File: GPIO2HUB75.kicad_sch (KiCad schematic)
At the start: 3 parts, among them J1 Conn_02x10_Odd_Even, J2 Conn_02x20_Odd_Even_MountingP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, J3 Conn_02x08_Top_Bottom

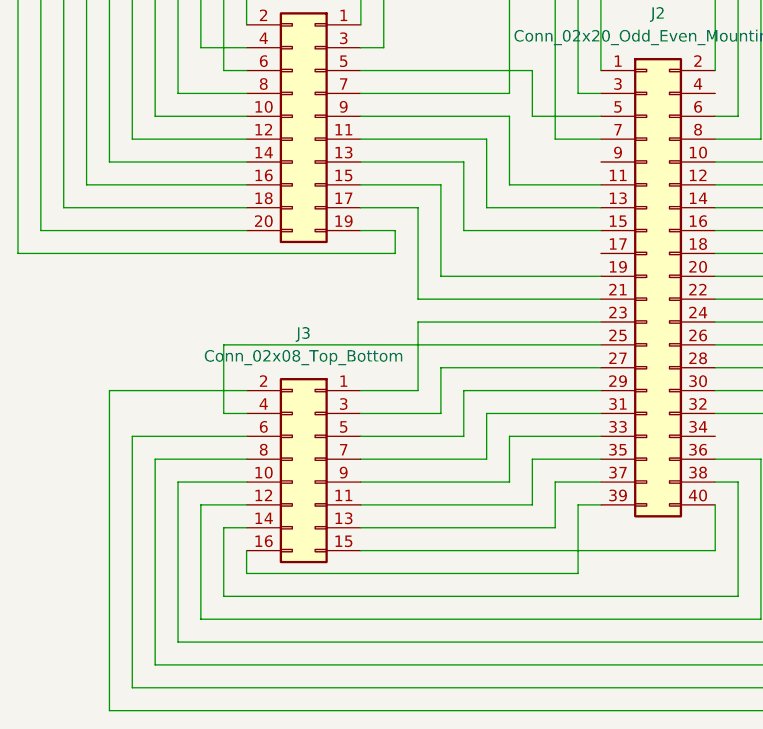
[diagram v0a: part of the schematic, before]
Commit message: added solder bridge to support 64x64+ panels
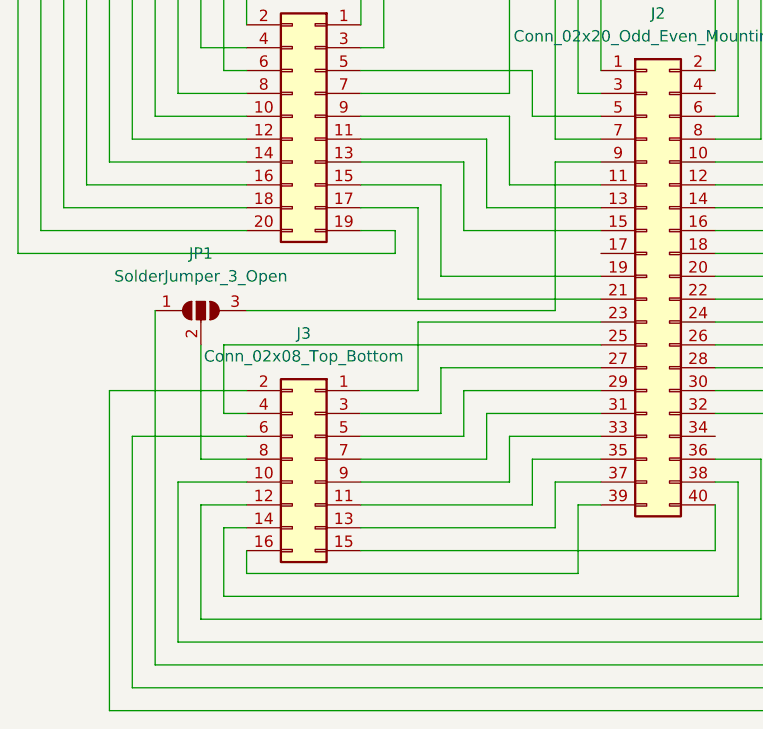
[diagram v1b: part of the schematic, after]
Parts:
- added JP1: SolderJumper_3_Open, Jumper:SolderJumper-3_P1.3mm_Open_Pad1.0x1.5mm_NumberLabels, symbol Jumper:SolderJumper_3_Open
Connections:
- net at J2.28 (Pin_28): now also JP1.1 (A); no longer J3.8 (Pin_8)
- net at J2.9 (Pin_9): now also JP1.3 (B)
- new net: J3.8 (Pin_8), JP1.2 (C)
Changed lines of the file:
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@@
+    (stroke (width 0) (type default))
+  )
+  (wire (pts (xy 193.04 72.39) (xy 187.96 72.39))
     (stroke (width 0) (type default))
   )
@@
     (stroke (width 0) (type default))
   )
-  (wire (pts (xy 143.51 105.41) (xy 143.51 128.27))
-    (stroke (width 0) (type default))
-  )
   (wire (pts (xy 205.74 62.23) (xy 205.74 48.26))
     (stroke (width 0) (type default))
@@
     (stroke (width 0) (type default))
   )
-  (wire (pts (xy 143.51 105.41) (xy 153.67 105.41))
-    (stroke (width 0) (type default))
-  )
   (wire (pts (xy 185.42 62.23) (xy 166.37 62.23))
     (stroke (width 0) (type default))
@@
     (stroke (width 0) (type default))
   )
+  (wire (pts (xy 148.59 105.41) (xy 153.67 105.41))
+    (stroke (width 0) (type default))
+  )
   (wire (pts (xy 205.74 90.17) (xy 220.98 90.17))
     (stroke (width 0) (type default))
@@
     (stroke (width 0) (type default))
   )
+  (wire (pts (xy 143.51 88.9) (xy 143.51 128.27))
+    (stroke (width 0) (type default))
+  )
   (wire (pts (xy 193.04 62.23) (xy 193.04 45.72))
     (stroke (width 0) (type default))
@@
     (stroke (width 0) (type default))
   )
+  (wire (pts (xy 148.59 92.71) (xy 148.59 105.41))
+    (stroke (width 0) (type default))
+  )
   (wire (pts (xy 146.05 125.73) (xy 213.36 125.73))
     (stroke (width 0) (type default))
@@
     (stroke (width 0) (type default))
   )
+  (wire (pts (xy 153.67 88.9) (xy 187.96 88.9))
+    (stroke (width 0) (type default))
+  )
   (wire (pts (xy 170.18 80.01) (xy 166.37 80.01))
     (stroke (width 0) (type default))
   )
+  (wire (pts (xy 187.96 72.39) (xy 187.96 88.9))
+    (stroke (width 0) (type default))
+  )
   (wire (pts (xy 135.89 27.94) (xy 135.89 74.93))
     (stroke (width 0) (type default))
@@
     (stroke (width 0) (type default))
   )
+  (symbol (lib_id "Jumper:SolderJumper_3_Open") (at 148.59 88.9 0) (unit 1)
+    (in_bom yes) (on_board yes) (dnp no) (fields_autoplaced)
+    (property "Reference" "JP1" (at 148.59 82.55 0)
+      (effects (font (size 1.27 1.27)))
+    )
+    (property "Value" "SolderJumper_3_Open" (at 148.59 85.09 0)
+      (effects (font (size 1.27 1.27)))
+    )
+    (property "Footprint" "Jumper:SolderJumper-3_P1.3mm_Open_Pad1.0x1.5mm_NumberLabels" (at 148.59 88.9 0)
+      (effects (font (size 1.27 1.27)) hide)
+    )
+    (property "Datasheet" "~" (at 148.59 88.9 0)
+      (effects (font (size 1.27 1.27)) hide)
+    )
+    (pin "2")
+    (pin "1")
+    (pin "3")
+    (instances
+      (project "GPIO2HUB75"
+        (path "/1420b1a7-2230-482f-814a-7ef4eb1c7dc0"
+          (reference "JP1") (unit 1)
+        )
+      )
+    )
+  )
   (symbol (lib_id "Connector_Generic:Conn_02x08_Odd_Even") (at 161.29 105.41 0) (mirror y) (unit 1)

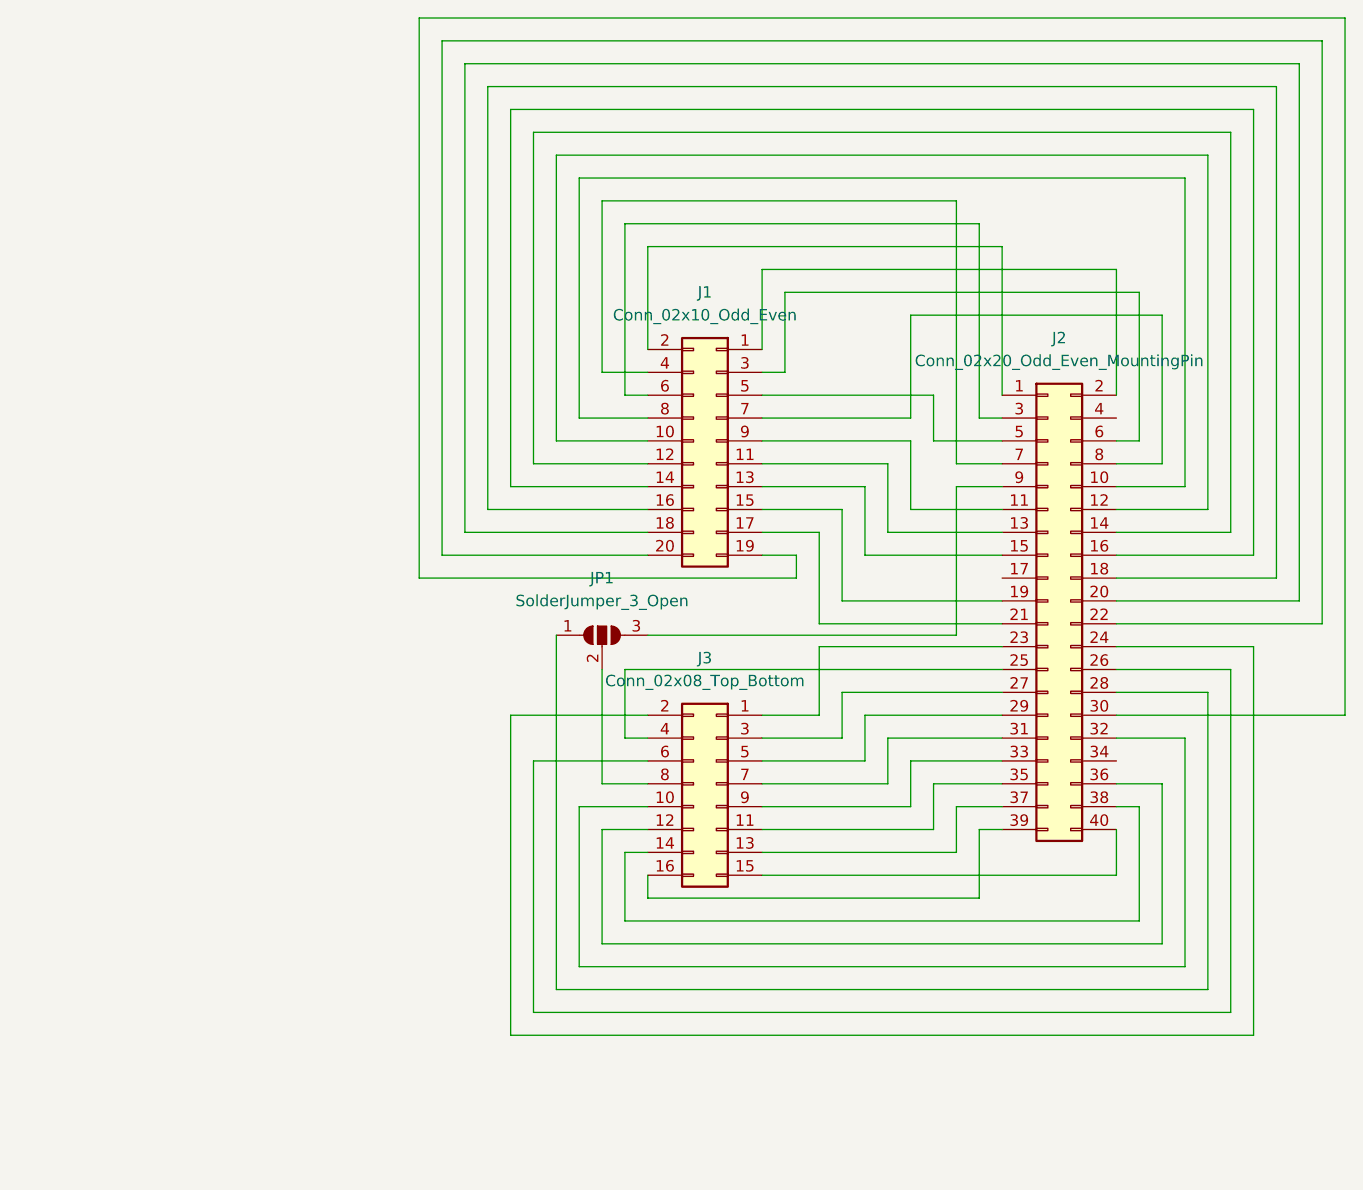
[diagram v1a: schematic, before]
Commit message: added a 3pin fan header
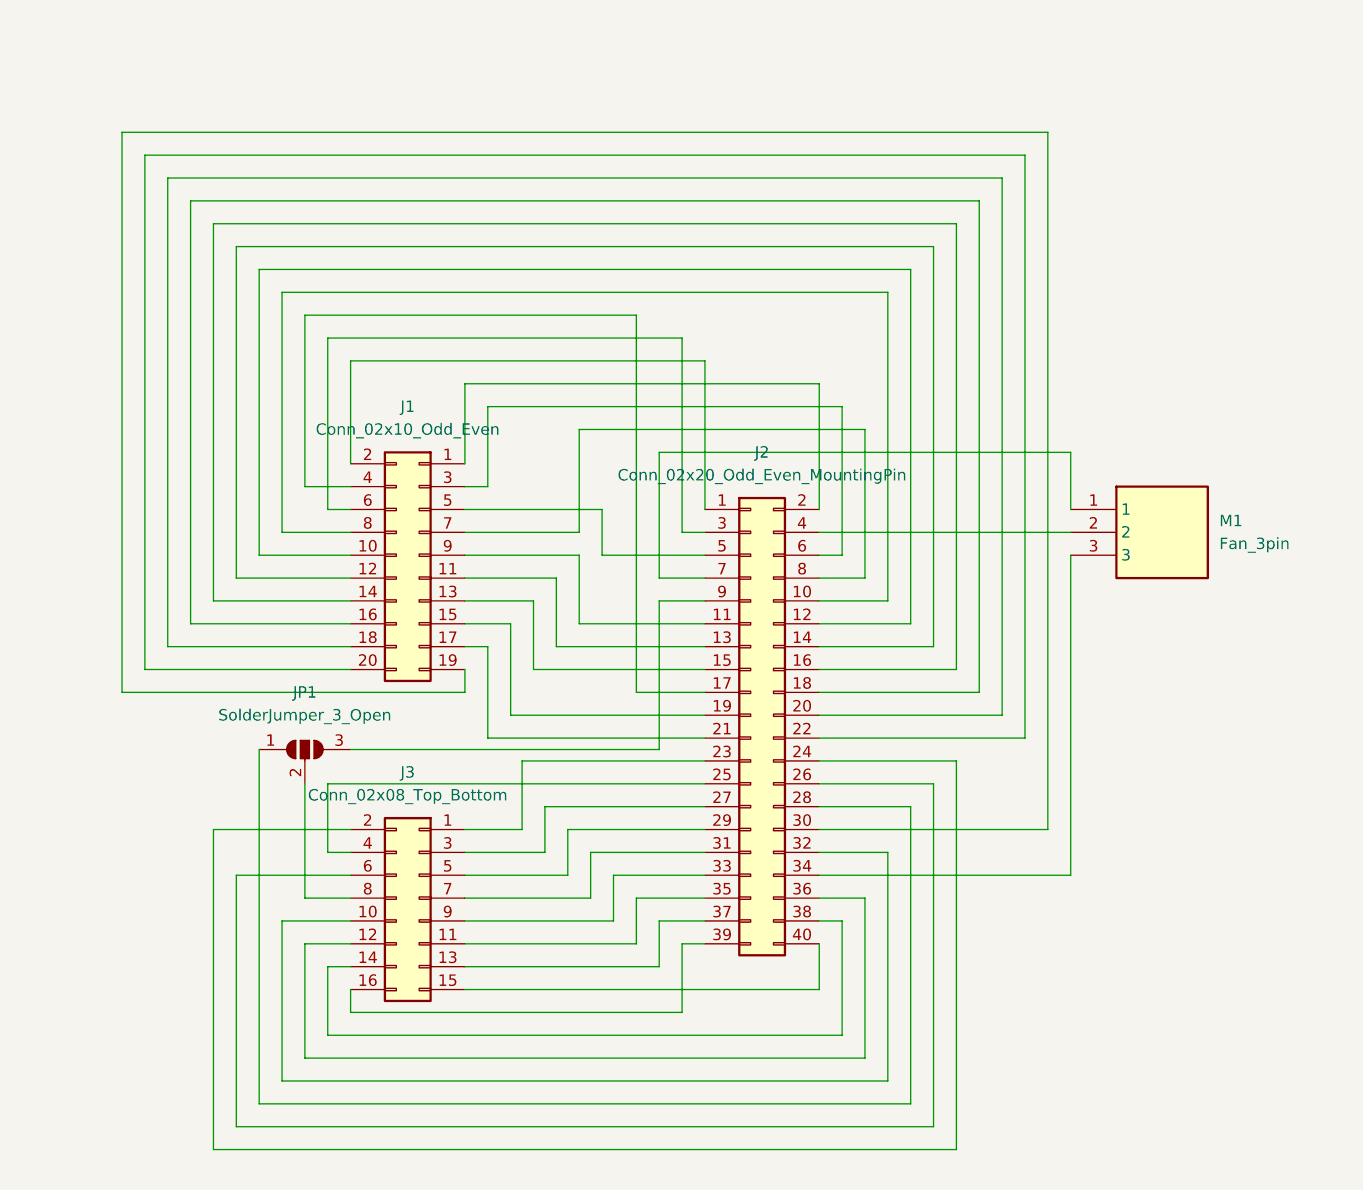
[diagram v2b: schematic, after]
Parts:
- added M1: Fan_3pin, 3 Pin Fan Header Angled:HDRRA3W64P0X254_1X3_747X318X635P, symbol 171857-3003:171857-3003
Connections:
- net at J2.17 (Pin_17): now also J1.4 (Pin_4)
- net at J2.34 (Pin_34): now also M1.3
- net at J2.4 (Pin_4): now also M1.2
- net at J2.7 (Pin_7): now also M1.1; no longer J1.4 (Pin_4)
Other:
- moved on the sheet: J1, J2, J3, JP1

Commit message: added a buzzer and split input pins from general GPIO
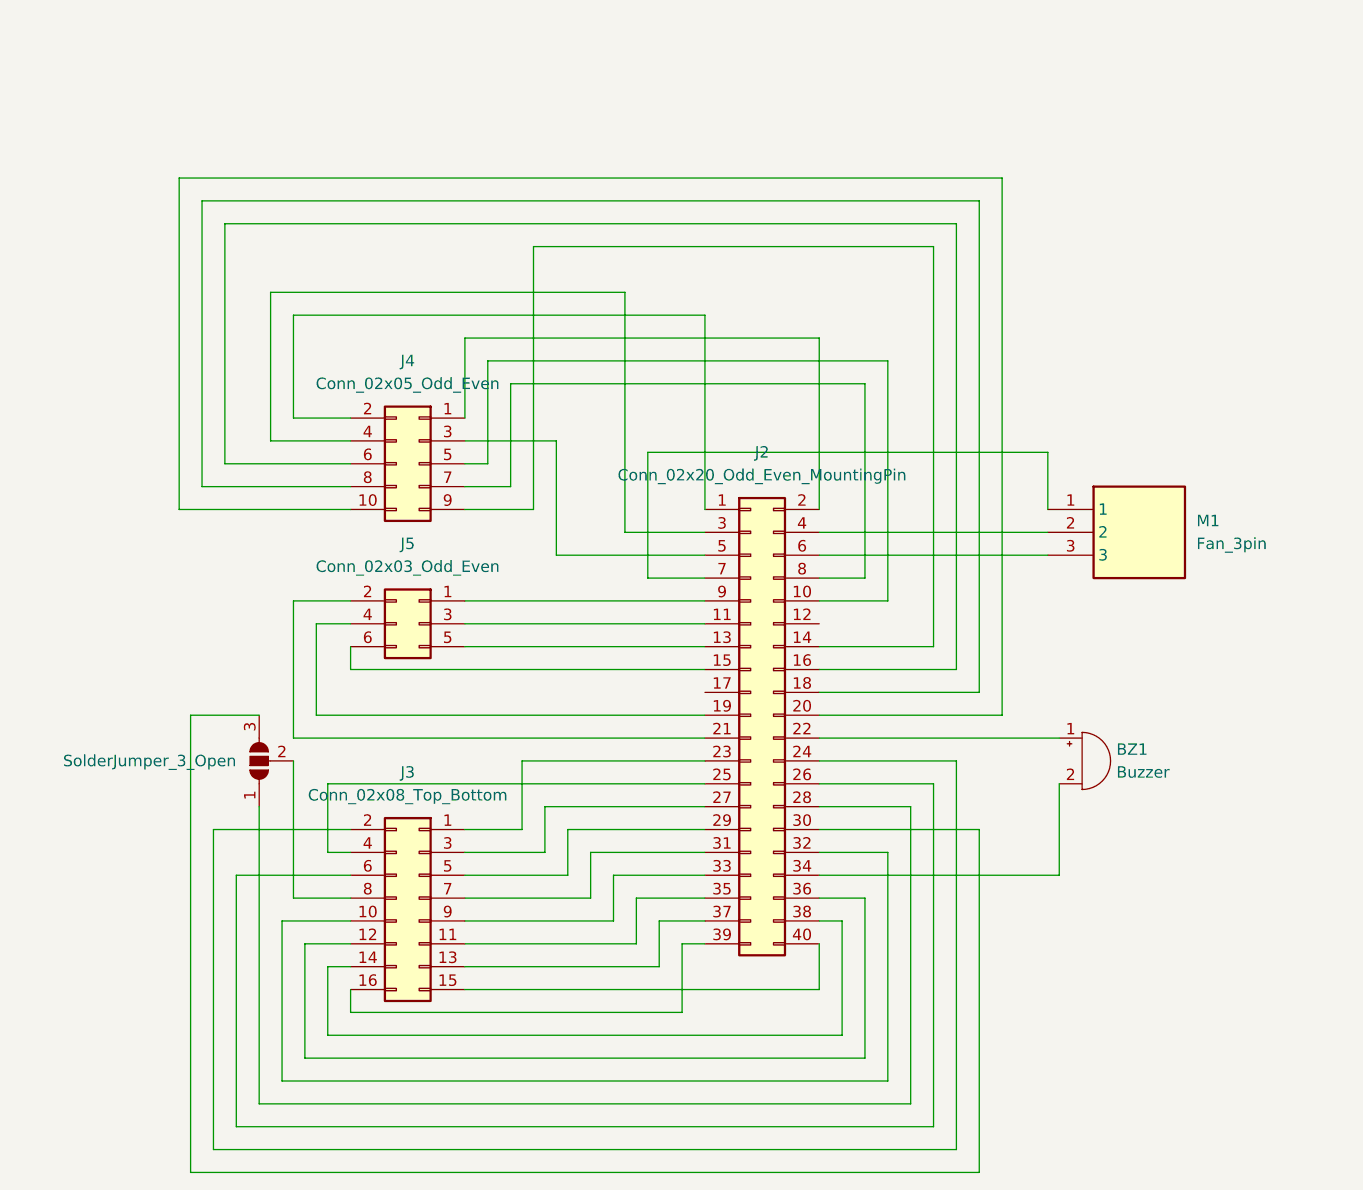
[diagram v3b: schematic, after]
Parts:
- removed J1: Conn_02x10_Odd_Even, Connector_PinHeader_2.54mm:PinHeader_2x10_P2.54mm_Horizontal, symbol Connector_Generic:Conn_02x10_Odd_Even
- added BZ1: Buzzer, Buzzer_Beeper:MagneticBuzzer_Kingstate_KCG0601, symbol Device:Buzzer
- added J4: Conn_02x05_Odd_Even, Connector_PinHeader_2.54mm:PinHeader_2x05_P2.54mm_Horizontal, symbol Connector_Generic:Conn_02x05_Odd_Even
- added J5: Conn_02x03_Odd_Even, Connector_IDC:IDC-Header_2x03_P2.54mm_Horizontal, symbol Connector_Generic:Conn_02x03_Odd_Even
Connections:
- net at J2.34 (Pin_34): now also BZ1.2 (+); no longer M1.3
- net at J2.9 (Pin_9): now also J5.1 (Pin_1); no longer JP1.3 (B)
- net at J2.1 (Pin_1): now also J4.2 (Pin_2)
- net at J2.10 (Pin_10): now also J4.5 (Pin_5)
- net at J2.11 (Pin_11): now also J5.3 (Pin_3)
- net at J2.13 (Pin_13): now also J5.5 (Pin_5)
- net at J2.14 (Pin_14): now also J4.9 (Pin_9)
- net at J2.15 (Pin_15): now also J5.6 (Pin_6)
- net at J2.16 (Pin_16): now also J4.6 (Pin_6)
- net at J2.18 (Pin_18): now also J4.8 (Pin_8)
- net at J2.19 (Pin_19): now also J5.4 (Pin_4)
- net at J2.2 (Pin_2): now also J4.1 (Pin_1)
- net at J2.20 (Pin_20): now also J4.10 (Pin_10)
- net at J2.21 (Pin_21): now also J5.2 (Pin_2)
- net at J2.22 (Pin_22): now also BZ1.1 (-)
- net at J2.3 (Pin_3): now also J4.4 (Pin_4)
- net at J2.30 (Pin_30): now also JP1.3 (B)
- net at J2.5 (Pin_5): now also J4.3 (Pin_3)
- net at J2.6 (Pin_6): now also M1.3
- net at J2.8 (Pin_8): now also J4.7 (Pin_7)
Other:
- moved on the sheet: M1

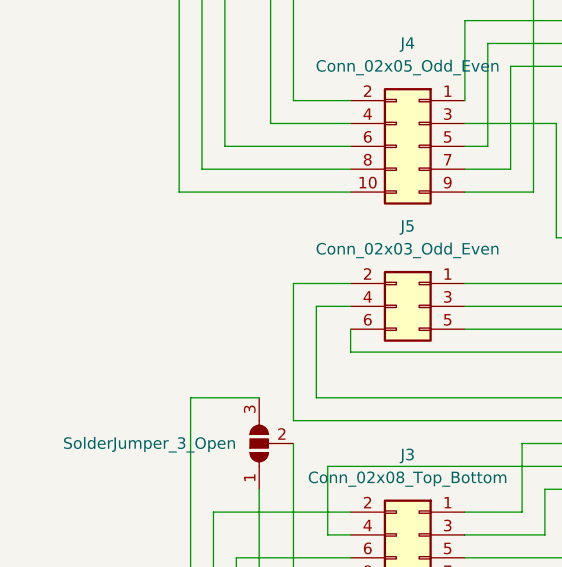
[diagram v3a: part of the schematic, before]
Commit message: added tilt sensor
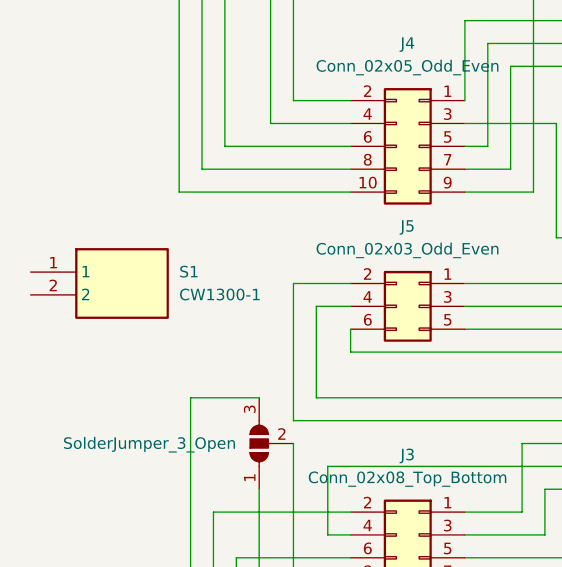
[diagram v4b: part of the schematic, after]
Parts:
- added S1: CW1300-1, Tilt Sensor:CW13001, symbol CW1300-1:CW1300-1
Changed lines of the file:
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@@
+    )
+  )
+  (symbol (lib_id "CW1300-1:CW1300-1") (at 85.09 83.82 0) (unit 1)
+    (in_bom yes) (on_board yes) (dnp no) (fields_autoplaced)
+    (property "Reference" "S1" (at 101.6 83.82 0)
+      (effects (font (size 1.27 1.27)) (justify left))
+    )
+    (property "Value" "CW1300-1" (at 101.6 86.36 0)
+      (effects (font (size 1.27 1.27)) (justify left))
+    )
+    (property "Footprint" "Tilt Sensor:CW13001" (at 101.6 178.74 0)
+      (effects (font (size 1.27 1.27)) (justify left top) hide)
+    )
+    (property "Datasheet" "" (at 101.6 278.74 0)
+      (effects (font (size 1.27 1.27)) (justify left top) hide)
+    )
+    (property "Height" "10.2" (at 101.6 478.74 0)
+      (effects (font (size 1.27 1.27)) (justify left top) hide)
+    )
+    (property "Farnell Part Number" "" (at 101.6 578.74 0)
+      (effects (font (size 1.27 1.27)) (justify left top) hide)
+    )
+    (property "Farnell Price/Stock" "" (at 101.6 678.74 0)
+      (effects (font (size 1.27 1.27)) (justify left top) hide)
+    )
+    (property "Manufacturer_Name" "Assemtech" (at 101.6 778.74 0)
+      (effects (font (size 1.27 1.27)) (justify left top) hide)
+    )
+    (property "Manufacturer_Part_Number" "CW1300-1" (at 101.6 878.74 0)
+      (effects (font (size 1.27 1.27)) (justify left top) hide)
+    )
+    (pin "1")
+    (pin "2")
+    (instances
+      (project "GPIO2HUB75"
+        (path "/1420b1a7-2230-482f-814a-7ef4eb1c7dc0"
+          (reference "S1") (unit 1)
+        )
+      )
     )
   )
